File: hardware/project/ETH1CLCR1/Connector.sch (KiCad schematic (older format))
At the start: 8 parts, among them J1601 C64AC, K1601 HE3621A0510, K1602 HE3621A0510, K1603 HE3621A0510, K1604 HE3621A0510, K1605 HE3621A0510, K1606 HE3621A0510, U1601 ULN2003A

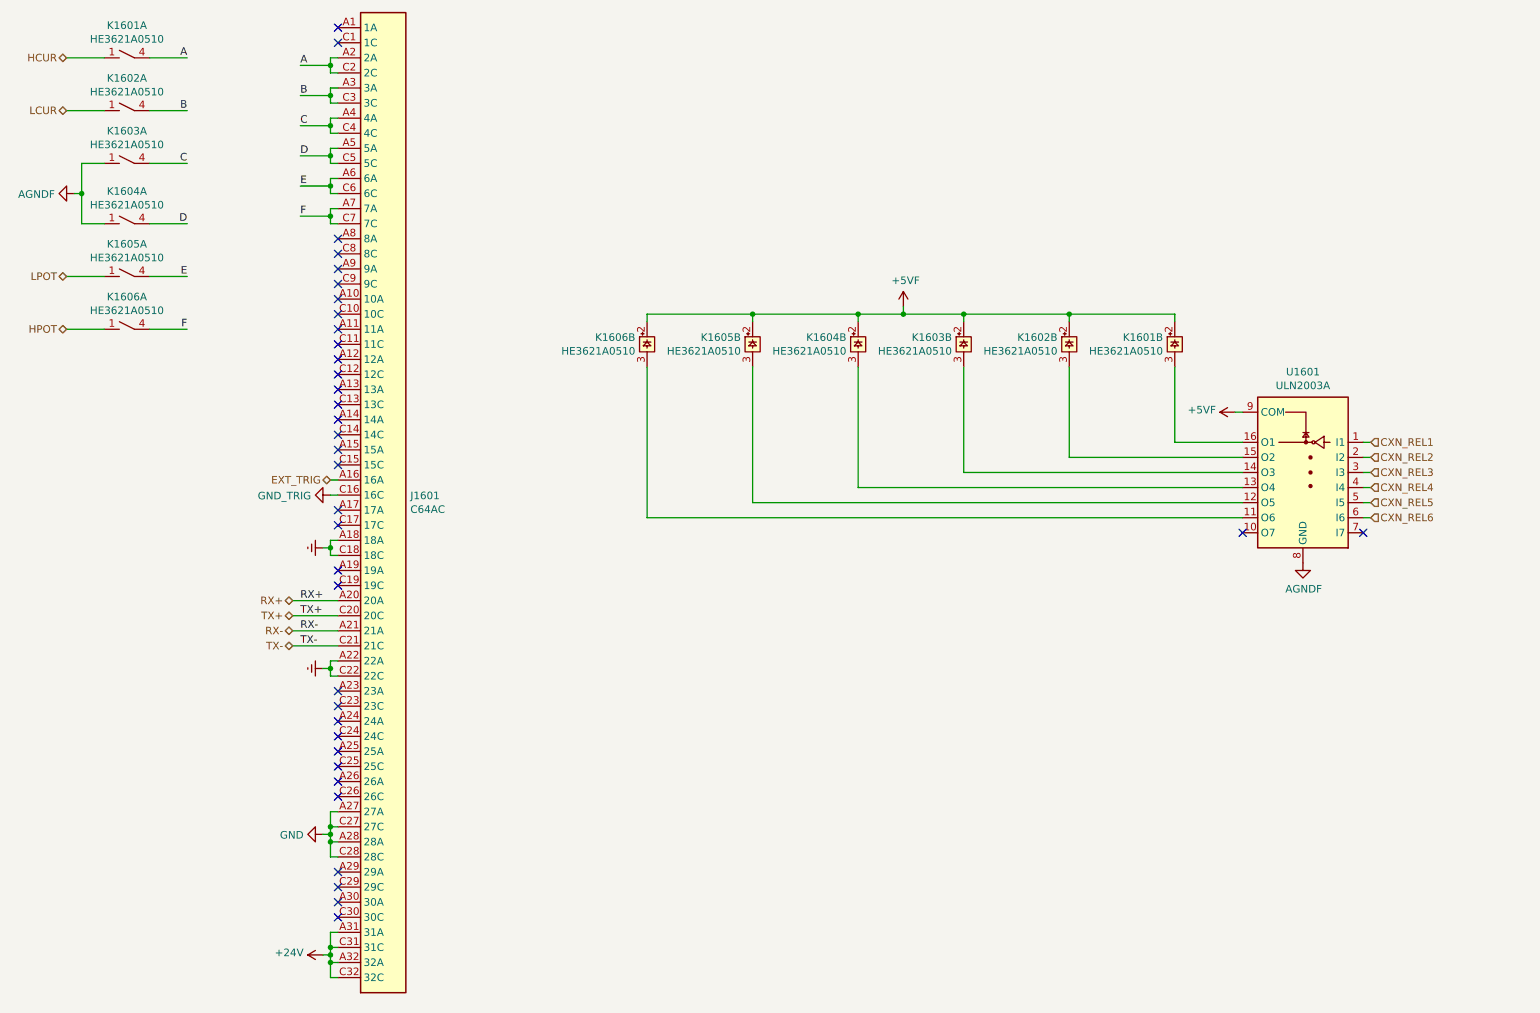
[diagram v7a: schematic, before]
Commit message: Redesigned the power supply, added humidy+temp. sensor.
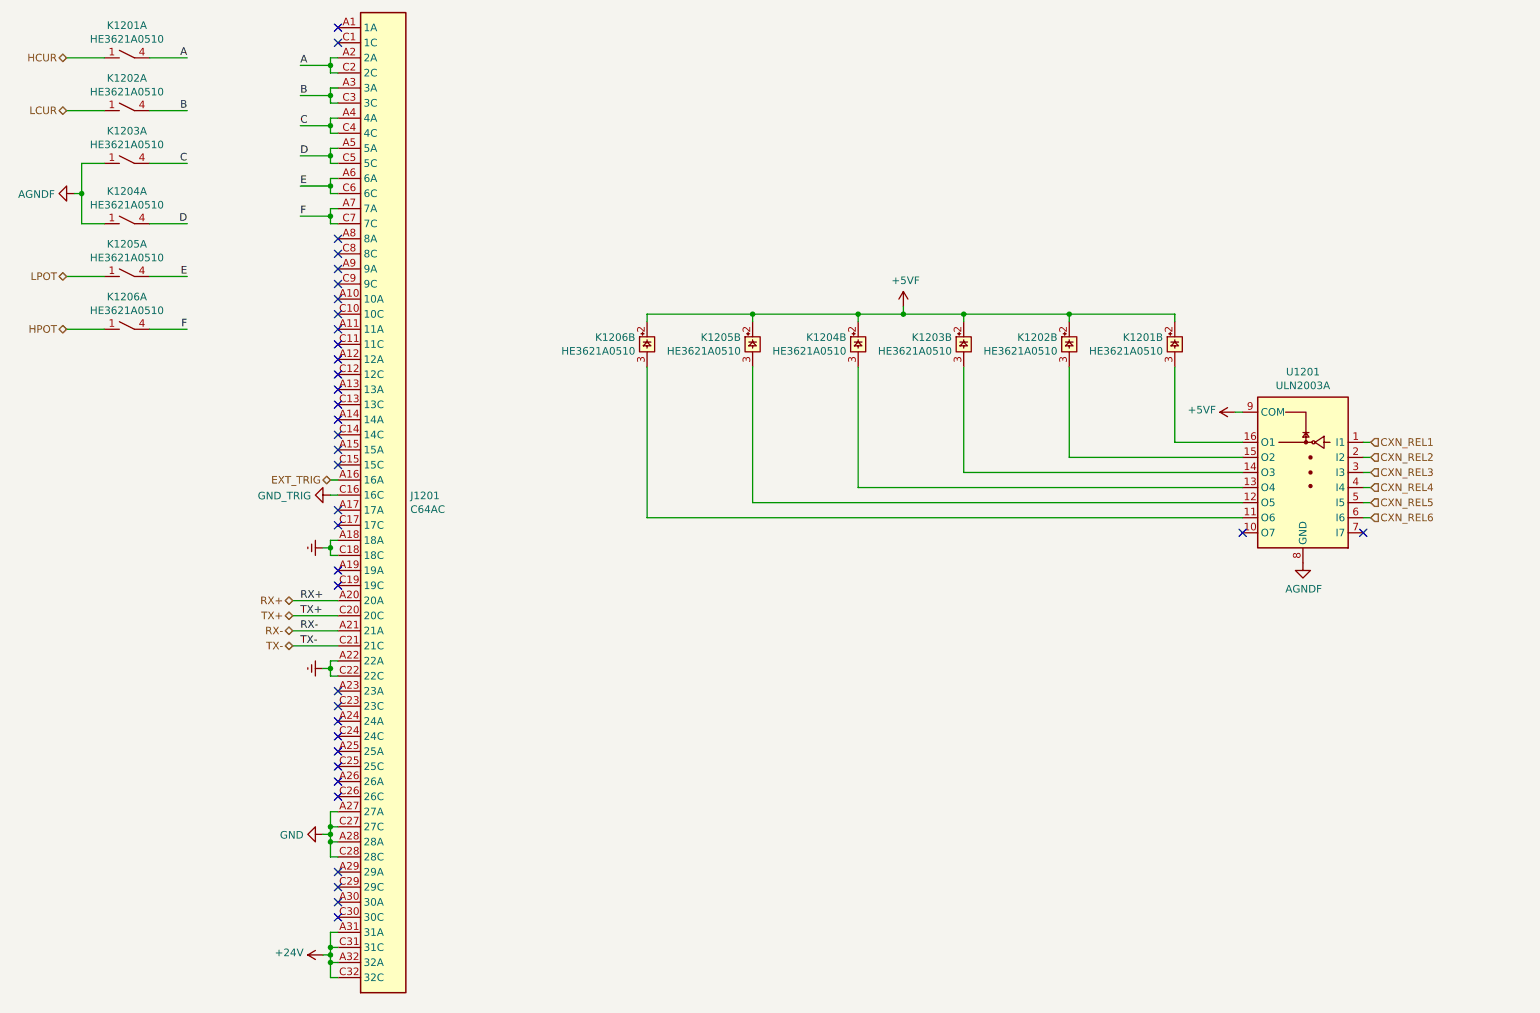
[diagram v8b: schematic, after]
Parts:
- renumbered J1601 to J1201, K1601 to K1201, K1602 to K1202, K1603 to K1203, K1604 to K1204, K1605 to K1205, K1606 to K1206, U1601 to U1201
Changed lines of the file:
@@
 $Descr A4 11693 8268
 encoding utf-8
-Sheet 16 16
+Sheet 12 15
 Title ""
 Date ""
@@
 Connection ~ 1450 2000
 $Comp
-L ETH1CLCR1:HE3621A0510 K1605
+L ETH1CLCR1:HE3621A0510 K1205
 U 1 1 5E1D650B
 P 1750 2550
-F 0 "K1605" V 1965 2550 50  0000 C CNN
+F 0 "K1205" V 1965 2550 50  0000 C CNN
 F 1 "HE3621A0510" V 1874 2550 50  0000 C CNN
 F 2 "ETH1CLCR1:HE360_x-5050462-8" H 2000 2500 50  0001 C CNN
@@
 $EndComp
 $Comp
-L ETH1CLCR1:HE3621A0510 K1604
+L ETH1CLCR1:HE3621A0510 K1204
 U 1 1 5E1D1D05
 P 1750 2200
-F 0 "K1604" V 1965 2200 50  0000 C CNN
+F 0 "K1204" V 1965 2200 50  0000 C CNN
 F 1 "HE3621A0510" V 1874 2200 50  0000 C CNN
 F 2 "ETH1CLCR1:HE360_x-5050462-8" H 2000 2150 50  0001 C CNN
@@
 $EndComp
 $Comp
-L ETH1CLCR1:HE3621A0510 K1603
+L ETH1CLCR1:HE3621A0510 K1203
 U 1 1 5E1CE0CF
 P 1750 1800
-F 0 "K1603" V 1965 1800 50  0000 C CNN
+F 0 "K1203" V 1965 1800 50  0000 C CNN
 F 1 "HE3621A0510" V 1874 1800 50  0000 C CNN
 F 2 "ETH1CLCR1:HE360_x-5050462-8" H 2000 1750 50  0001 C CNN
@@
 $EndComp
 $Comp
-L ETH1CLCR1:HE3621A0510 K1602
+L ETH1CLCR1:HE3621A0510 K1202
 U 1 1 5E1C97A7
 P 1750 1450
-F 0 "K1602" V 1965 1450 50  0000 C CNN
+F 0 "K1202" V 1965 1450 50  0000 C CNN
 F 1 "HE3621A0510" V 1874 1450 50  0000 C CNN
 F 2 "ETH1CLCR1:HE360_x-5050462-8" H 2000 1400 50  0001 C CNN
@@
 $EndComp
 $Comp
-L ETH1CLCR1:HE3621A0510 K1606
+L ETH1CLCR1:HE3621A0510 K1206
 U 1 1 5E1C5D93
 P 1750 2900
-F 0 "K1606" V 1965 2900 50  0000 C CNN
+F 0 "K1206" V 1965 2900 50  0000 C CNN
 F 1 "HE3621A0510" V 1874 2900 50  0000 C CNN
 F 2 "ETH1CLCR1:HE360_x-5050462-8" H 2000 2850 50  0001 C CNN
@@
 $EndComp
 $Comp
-L ETH1CLCR1:HE3621A0510 K1601
+L ETH1CLCR1:HE3621A0510 K1201
 U 1 1 5E1B6BE6
 P 1750 1100
-F 0 "K1601" V 1965 1100 50  0000 C CNN
+F 0 "K1201" V 1965 1100 50  0000 C CNN
 F 1 "HE3621A0510" V 1874 1100 50  0000 C CNN
 F 2 "ETH1CLCR1:HE360_x-5050462-8" H 2000 1050 50  0001 C CNN
@@
 F
 $Comp
-L ETH1CLCR1:AGNDF #PWR01601
+L ETH1CLCR1:AGNDF #PWR01201
 U 1 1 5E36903D
 P 1400 2000
-F 0 "#PWR01601" H 1400 1750 50  0001 C CNN
+F 0 "#PWR01201" H 1400 1750 50  0001 C CNN
 F 1 "AGNDF" V 1405 1872 50  0000 R CNN
 F 2 "" H 1400 2000 50  0001 C CNN
@@
 	3100 4000 3150 4000
 $Comp
-L ETH1CLCR1:GND_TRIG #PWR01606
+L ETH1CLCR1:GND_TRIG #PWR01206
 U 1 1 5EC065BC
 P 3100 4000
-F 0 "#PWR01606" H 3100 3750 50  0001 C CNN
+F 0 "#PWR01206" H 3100 3750 50  0001 C CNN
 F 1 "GND_TRIG" V 3105 3872 50  0000 R CNN
 F 2 "" H 3100 4000 50  0001 C CNN
@@
 	3050 4350 3100 4350
 $Comp
-L power:Earth #PWR01602
+L power:Earth #PWR01202
 U 1 1 5DED2C4C
 P 3050 4350
-F 0 "#PWR01602" H 3050 4100 50  0001 C CNN
+F 0 "#PWR01202" H 3050 4100 50  0001 C CNN
 F 1 "Earth" H 3050 4200 50  0001 C CNN
 F 2 "" H 3050 4350 50  0001 C CNN
@@
 	3050 5150 3100 5150
 $Comp
-L power:Earth #PWR01603
+L power:Earth #PWR01203
 U 1 1 5DECE77F
 P 3050 5150
-F 0 "#PWR01603" H 3050 4900 50  0001 C CNN
+F 0 "#PWR01203" H 3050 4900 50  0001 C CNN
 F 1 "Earth" H 3050 5000 50  0001 C CNN
 F 2 "" H 3050 5150 50  0001 C CNN
@@
 	3050 6250 3100 6250
 $Comp
-L power:GND #PWR01604
+L power:GND #PWR01204
 U 1 1 5DE992F4
 P 3050 6250
-F 0 "#PWR01604" H 3050 6000 50  0001 C CNN
+F 0 "#PWR01204" H 3050 6000 50  0001 C CNN
 F 1 "GND" V 3055 6122 50  0000 R CNN
 F 2 "" H 3050 6250 50  0001 C CNN
@@
 	3050 7050 3100 7050
 $Comp
-L power:+24V #PWR01605
+L power:+24V #PWR01205
 U 1 1 5DE97137
 P 3050 7050
-F 0 "#PWR01605" H 3050 6900 50  0001 C CNN
+F 0 "#PWR01205" H 3050 6900 50  0001 C CNN
 F 1 "+24V" V 3065 7178 50  0000 L CNN
 F 2 "" H 3050 7050 50  0001 C CNN
@@
 	3150 7200 3100 7200
 $Comp
-L Connector:C64AC J1601
+L Connector:C64AC J1201
 U 1 1 5DE8758D
 P 3450 4100
-F 0 "J1601" H 3630 4196 50  0000 L CNN
+F 0 "J1201" H 3630 4196 50  0000 L CNN
 F 1 "C64AC" H 3630 4105 50  0000 L CNN
 F 2 "ETH1CLCR1:Socket_DIN41612-CaseC1-AC-Male-64Pin-2rows" H 3450 4150 50  0001 C CNN
@@
 $EndComp
 $Comp
-L ETH1CLCR1:AGNDF #PWR01609
+L ETH1CLCR1:AGNDF #PWR01209
 U 1 1 5E675EDD
 P 9550 4450
-F 0 "#PWR01609" H 9550 4200 50  0001 C CNN
+F 0 "#PWR01209" H 9550 4200 50  0001 C CNN
 F 1 "AGNDF" H 9555 4277 50  0000 C CNN
 F 2 "" H 9550 4450 50  0001 C CNN
@@
 	6900 2750 6900 2800
 $Comp
-L ETH1CLCR1:+5VF #PWR01607
+L ETH1CLCR1:+5VF #PWR01207
 U 1 1 5E5FEFEE
 P 6900 2750
-F 0 "#PWR01607" H 6900 2600 50  0001 C CNN
+F 0 "#PWR01207" H 6900 2600 50  0001 C CNN
 F 1 "+5VF" H 6915 2923 50  0000 C CNN
 F 2 "" H 6900 2750 50  0001 C CNN
@@
 	9100 3450 9150 3450
 $Comp
-L ETH1CLCR1:+5VF #PWR01608
+L ETH1CLCR1:+5VF #PWR01208
 U 1 1 5E521985
 P 9100 3450
-F 0 "#PWR01608" H 9100 3300 50  0001 C CNN
+F 0 "#PWR01208" H 9100 3300 50  0001 C CNN
 F 1 "+5VF" V 9115 3577 50  0000 L CNN
 F 2 "" H 9100 3450 50  0001 C CNN
@@
 $EndComp
 $Comp
-L Transistor_Array:ULN2003A U1601
+L Transistor_Array:ULN2003A U1201
 U 1 1 5E4D3152
 P 9550 3850
-F 0 "U1601" H 9550 4517 50  0000 C CNN
+F 0 "U1201" H 9550 4517 50  0000 C CNN
 F 1 "ULN2003A" H 9550 4426 50  0000 C CNN
 F 2 "Package_SO:TSSOP-16_4.4x5mm_P0.65mm" H 9600 3300 50  0001 L CNN
@@
 CXN_REL4
 $Comp
-L ETH1CLCR1:HE3621A0510 K1605
+L ETH1CLCR1:HE3621A0510 K1205
 U 2 1 5E1D6511
 P 5900 3000
-F 0 "K1605" H 5978 3046 50  0000 L CNN
+F 0 "K1205" H 5978 3046 50  0000 L CNN
 F 1 "HE3621A0510" H 5978 2955 50  0000 L CNN
 F 2 "ETH1CLCR1:HE360_x-5050462-8" H 6150 2950 50  0001 C CNN
@@
 $EndComp
 $Comp
-L ETH1CLCR1:HE3621A0510 K1604
+L ETH1CLCR1:HE3621A0510 K1204
 U 2 1 5E1D1D0B
 P 6600 3000
-F 0 "K1604" H 6678 3046 50  0000 L CNN
+F 0 "K1204" H 6678 3046 50  0000 L CNN
 F 1 "HE3621A0510" H 6678 2955 50  0000 L CNN
 F 2 "ETH1CLCR1:HE360_x-5050462-8" H 6850 2950 50  0001 C CNN
@@
 $EndComp
 $Comp
-L ETH1CLCR1:HE3621A0510 K1603
+L ETH1CLCR1:HE3621A0510 K1203
 U 2 1 5E1CE0D5
 P 7300 3000
-F 0 "K1603" H 7378 3046 50  0000 L CNN
+F 0 "K1203" H 7378 3046 50  0000 L CNN
 F 1 "HE3621A0510" H 7378 2955 50  0000 L CNN
 F 2 "ETH1CLCR1:HE360_x-5050462-8" H 7550 2950 50  0001 C CNN
@@
 $EndComp
 $Comp
-L ETH1CLCR1:HE3621A0510 K1602
+L ETH1CLCR1:HE3621A0510 K1202
 U 2 1 5E1C97AD
 P 8000 3000
-F 0 "K1602" H 8078 3046 50  0000 L CNN
+F 0 "K1202" H 8078 3046 50  0000 L CNN
 F 1 "HE3621A0510" H 8078 2955 50  0000 L CNN
 F 2 "ETH1CLCR1:HE360_x-5050462-8" H 8250 2950 50  0001 C CNN
@@
 $EndComp
 $Comp
-L ETH1CLCR1:HE3621A0510 K1606
+L ETH1CLCR1:HE3621A0510 K1206
 U 2 1 5E1C5D99
 P 5200 3000
-F 0 "K1606" H 5278 3046 50  0000 L CNN
+F 0 "K1206" H 5278 3046 50  0000 L CNN
 F 1 "HE3621A0510" H 5278 2955 50  0000 L CNN
 F 2 "ETH1CLCR1:HE360_x-5050462-8" H 5450 2950 50  0001 C CNN
@@
 $EndComp
 $Comp
-L ETH1CLCR1:HE3621A0510 K1601
+L ETH1CLCR1:HE3621A0510 K1201
 U 2 1 5E1C1048
 P 8700 3000
-F 0 "K1601" H 8778 3046 50  0000 L CNN
+F 0 "K1201" H 8778 3046 50  0000 L CNN
 F 1 "HE3621A0510" H 8778 2955 50  0000 L CNN
 F 2 "ETH1CLCR1:HE360_x-5050462-8" H 8950 2950 50  0001 C CNN
